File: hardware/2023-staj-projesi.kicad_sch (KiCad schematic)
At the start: 1 part, among them J1 Screw_Terminal_01x03

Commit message: LCD module completed
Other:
- sheet LCD ports: added SCL, SDA; removed none
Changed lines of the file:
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@@
       (effects (font (size 1.27 1.27)) (justify left top))
+    )
+    (pin "SCL" input (at 70.485 66.04 0)
+      (effects (font (size 1.27 1.27)) (justify right))
+    )
+    (pin "SDA" bidirectional (at 70.485 68.58 0)
+      (effects (font (size 1.27 1.27)) (justify right))
     )
     (instances

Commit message: GSM module completed
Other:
- sheet GSM ports: added RXD, TXD; removed none
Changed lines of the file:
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@@
       (effects (font (size 1.27 1.27)) (justify left top))
+    )
+    (pin "TXD" output (at 71.12 107.95 0)
+      (effects (font (size 1.27 1.27)) (justify right))
+    )
+    (pin "RXD" input (at 71.12 105.41 0)
+      (effects (font (size 1.27 1.27)) (justify right))
     )
     (instances

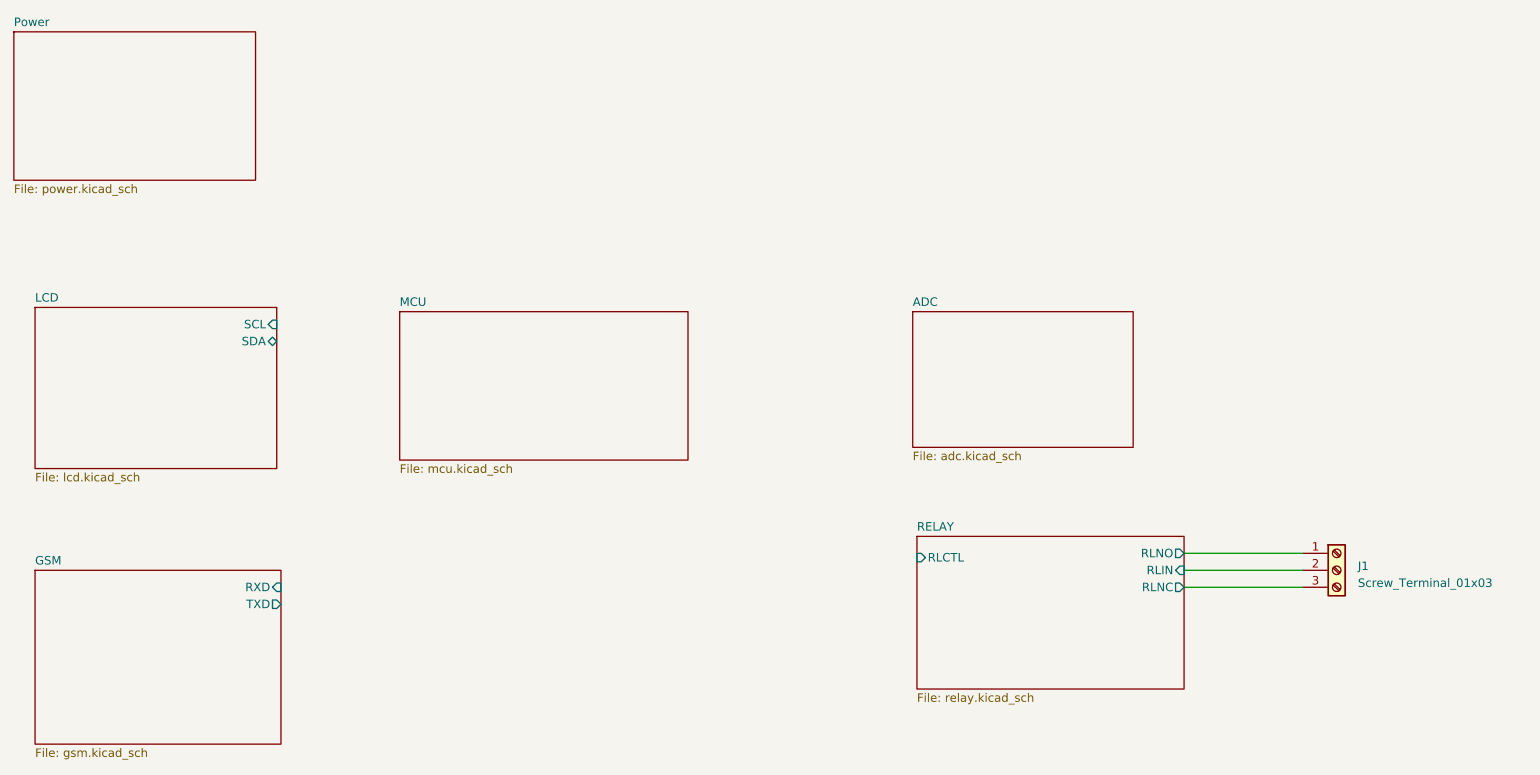
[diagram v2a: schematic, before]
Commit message: * Added an EXP port (contains SPI/I2C/UART/2PINS GPIO/3V3/5V) to the MCU module * USB port connections completed * The Modules are connected to MCU module
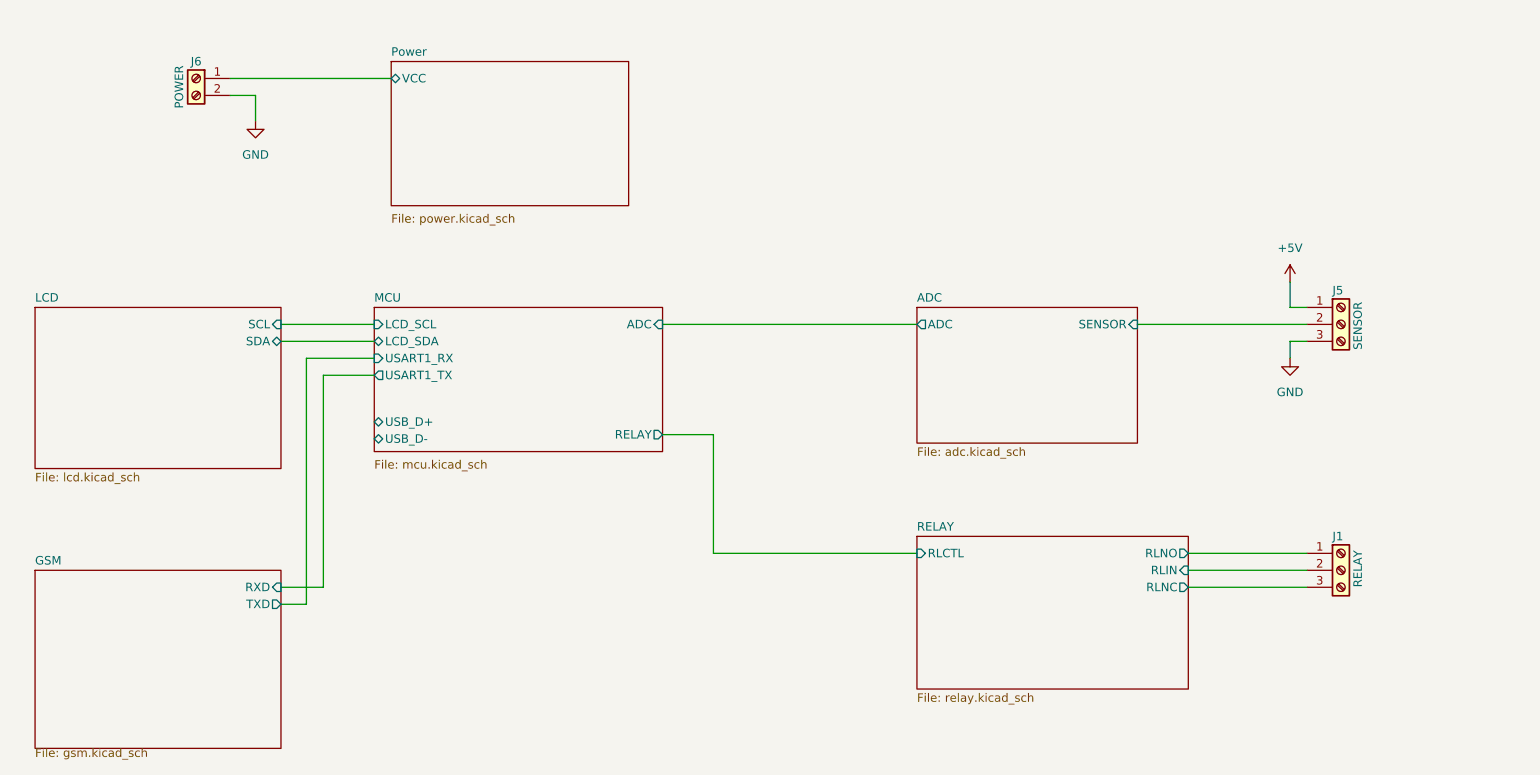
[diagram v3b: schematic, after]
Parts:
- added J5: SENSOR, symbol Connector:Screw_Terminal_01x03
- added J6: POWER, symbol Connector:Screw_Terminal_01x02
- J1: value Screw_Terminal_01x03 -> RELAY
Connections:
- new net +5V: J5.1 (Pin_1)
- new net ADC/SENSOR: J5.2 (Pin_2)
- new net GND: J5.3 (Pin_3), J6.2 (Pin_2)
- new net Power/VCC: J6.1 (Pin_1)
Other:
- sheet ADC ports: added ADC, SENSOR; removed none
- sheet MCU ports: added ADC, LCD_SCL, LCD_SDA, RELAY, USART1_RX, USART1_TX, USB_D+, USB_D-; removed none
- sheet Power ports: added VCC; removed none
- moved on the sheet: J1

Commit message: Power modules completed except 3V8
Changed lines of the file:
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@@
-    (stroke (width 0) (type default))
-  )
-  (wire (pts (xy 224.79 63.5) (xy 222.25 63.5))
     (stroke (width 0) (type default))
   )
@@
     (stroke (width 0) (type default))
   )
-  (wire (pts (xy 222.25 63.5) (xy 222.25 59.69))
+  (wire (pts (xy 222.25 63.5) (xy 224.79 63.5))
     (stroke (width 0) (type default))
   )
@@
     (stroke (width 0) (type default))
   )
+  (wire (pts (xy 222.25 59.69) (xy 222.25 63.5))
+    (stroke (width 0) (type default))
+  )
